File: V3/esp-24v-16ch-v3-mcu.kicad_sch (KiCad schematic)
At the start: 14 parts, among them Q3 UMH3N, SW1 RESET, U3 CH340C, U4 ESP32-WROOM-32UE-N16

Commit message: working on v3
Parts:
- C11: value 10uF/10V/0603 -> 10uF/10V
- C12: value 0,1uF/50V/0805 -> 0,1uF/50V; footprint Tales:C_0805_2012Metric -> Tales:C_0402_1005Metric; Case 0805/2012 -> 0402/1005; LCSC Part # C49678 -> C307331; Mfr Yageo -> Samsung; Mfr PN CC0805KRX7R9BB104 -> CL05B104KB54PNC; Package (none) -> 0402/1005; Technology Ceramic -> Ceramic X7R; Vendor PN C49678 -> C307331
- C13: value 1uF/50V/0603 -> 1uF/25V; footprint Tales:C_0603_1608Metric -> Tales:C_0402_1005Metric; Case 0603/1608 -> 0402/1005; LCSC Part # C15849 -> C52923; Mfr PN CL10A105KB8NNNC -> CL05A105KA5NQNC; Package (none) -> 0402/1005; Vendor PN C15849 -> C52923
- R10, R11, R12: value 10k/62,5mW/0402 -> 10k/62,5mW; LCSC Part # C25744 -> C60490; Mfr Uniroyal -> Yageo; Mfr PN 0402WGF1002TCE -> RC0402FR-0710KL; Package (none) -> 0402/1005; Technology (none) -> 1%; Vendor PN C25744 -> C60490
- R129, R13, R130, R14: value 2k2/62,5mW/0402 -> 2k2/62,5mW
- U4: value ESP32-WROOM-32UE-N16 -> ESP32-WROOM-32UE-N4; LCSC Part # C701346 -> C701344; Mfr PN ESP32-WROOM-32UE-N16 -> ESP32-WROOM-32UE-N4; Vendor PN C701346 -> C701344

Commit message: Final adjustments before production
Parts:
- removed U3: CH340C, Tales:SOIC-16_3.9x9.9mm_P1.27mm, symbol Interface_USB:CH340C
- added U3: CH340C, Package_SO:SOIC-16_3.9x9.9mm_P1.27mm, symbol Tales:CH340C
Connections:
- net +3.3V: now also U3.16 (VCC), U3.4 (V3)
- net GND: now also U3.1 (GND)
- net USB_D+: now also U3.5 (UD+)
- net USB_D-: now also U3.6 (UD-)
- net at Q3.2 (B1), Q3.4 (E2): now also U3.13 (~{DTR})
- net at Q3.1 (E1), Q3.5 (B2): now also U3.14 (~{RTS})
- net at U4.34 (RXD0/IO3): now also U3.2 (TXD)
- net at U4.35 (TXD0/IO1): now also U3.3 (RXD)

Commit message: Added temperature sensor
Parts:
- C12: value 0,1uF/50V -> 100nF/50V
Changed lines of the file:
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@@
 			)
 		)
-		(property "Value" "0,1uF/50V"
+		(property "Value" "100nF/50V"
 			(at 45.72 60.9662 0)
 			(effects

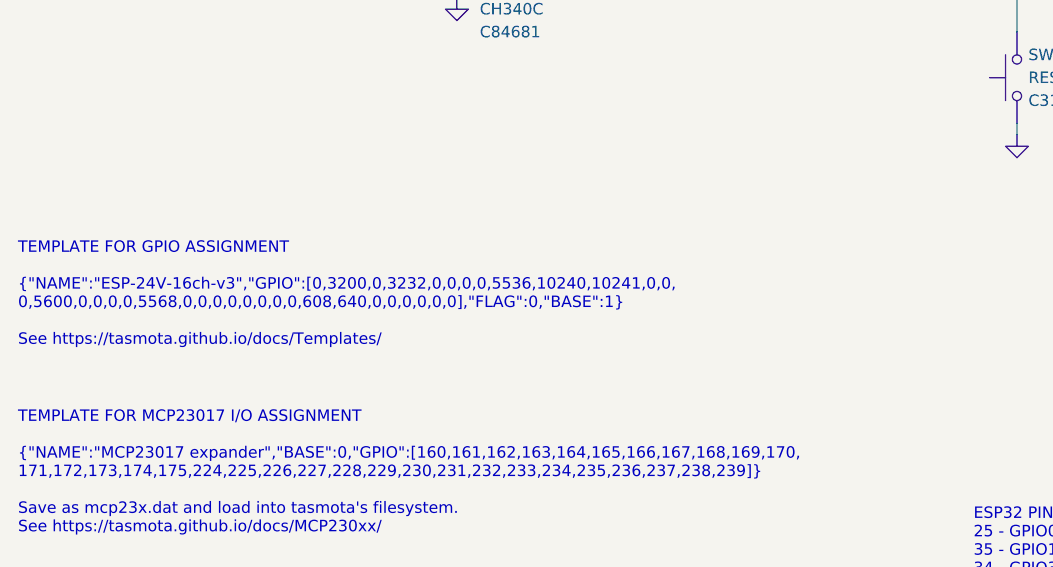
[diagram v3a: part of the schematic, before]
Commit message: Update esp-24v-16ch-v3-mcu.kicad_sch
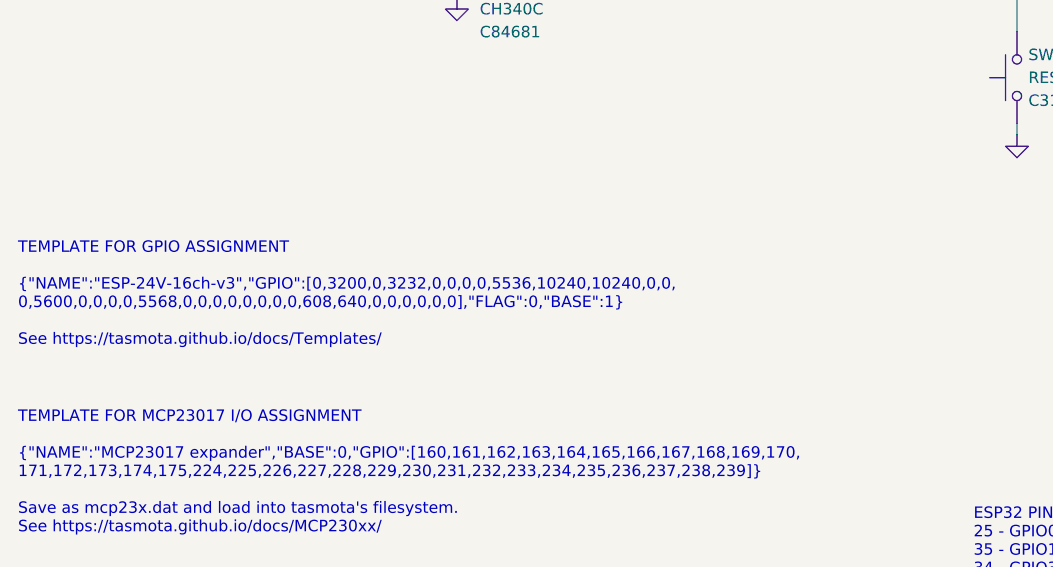
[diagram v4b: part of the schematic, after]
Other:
- note added: "TEMPLATE FOR GPIO ASSIGNMENT {"NAME":"ESP-24V-16ch-v3","GPIO":[0,3200,0,3232,0,0,0,0,5536,10240,10240,0,0, 0,5600,0,0,0,0,5568,0,0,0,0,0,0,0,0,608,640,0,0,0,0,0,0],"FLAG":0,"BASE":1} See https://tasmota.github.io/docs/Templates/"
- note removed: "TEMPLATE FOR GPIO ASSIGNMENT {"NAME":"ESP-24V-16ch-v3","GPIO":[0,3200,0,3232,0,0,0,0,5536,10240,10241,0,0, 0,5600,0,0,0,0,5568,0,0,0,0,0,0,0,0,608,640,0,0,0,0,0,0],"FLAG":0,"BASE":1} See https://tasmota.github.io/docs/Templates/"
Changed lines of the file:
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@@
 		)
 	)
-	(text "TEMPLATE FOR GPIO ASSIGNMENT\n\n{\"NAME\":\"ESP-24V-16ch-v3\",\"GPIO\":[0,3200,0,3232,0,0,0,0,5536,10240,10241,0,0,\n0,5600,0,0,0,0,5568,0,0,0,0,0,0,0,0,608,640,0,0,0,0,0,0],\"FLAG\":0,\"BASE\":1}\n\nSee https://tasmota.github.io/docs/Templates/"
+	(text "TEMPLATE FOR GPIO ASSIGNMENT\n\n{\"NAME\":\"ESP-24V-16ch-v3\",\"GPIO\":[0,3200,0,3232,0,0,0,0,5536,10240,10240,0,0,\n0,5600,0,0,0,0,5568,0,0,0,0,0,0,0,0,608,640,0,0,0,0,0,0],\"FLAG\":0,\"BASE\":1}\n\nSee https://tasmota.github.io/docs/Templates/"
 		(exclude_from_sim no)
 		(at 14.732 141.732 0)

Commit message: Updated footprints
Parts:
- U3: footprint Package_SO:SOIC-16_3.9x9.9mm_P1.27mm -> Tales:SOIC-16_3.9x9.9mm_P1.27mm
- U4: value ESP32-WROOM-32UE-N4 -> ESP32-WROOM-32UE-N16; LCSC Part # C701344 -> C701346; Mfr PN ESP32-WROOM-32UE-N4 -> ESP32-WROOM-32UE-N16; Vendor PN C701344 -> C701346
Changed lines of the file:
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@@
 			)
 		)
-		(property "Footprint" "Package_SO:SOIC-16_3.9x9.9mm_P1.27mm"
+		(property "Footprint" "Tales:SOIC-16_3.9x9.9mm_P1.27mm"
 			(at 44.958 56.134 0)
 			(effects
@@
 			)
 		)
-		(property "Value" "ESP32-WROOM-32UE-N4"
+		(property "Value" "ESP32-WROOM-32UE-N16"
 			(at 182.88 148.59 0)
 			(effects
@@
 			)
 		)
-		(property "LCSC Part #" "C701344"
+		(property "LCSC Part #" "C701346"
 			(at 182.88 151.13 0)
 			(effects
@@
 			)
 		)
-		(property "Mfr PN" "ESP32-WROOM-32UE-N4"
+		(property "Mfr PN" "ESP32-WROOM-32UE-N16"
 			(at 179.07 110.49 0)
 			(effects
@@
 			)
 		)
-		(property "Vendor PN" "C701344"
+		(property "Vendor PN" "C701346 "
 			(at 179.07 110.49 0)
 			(effects

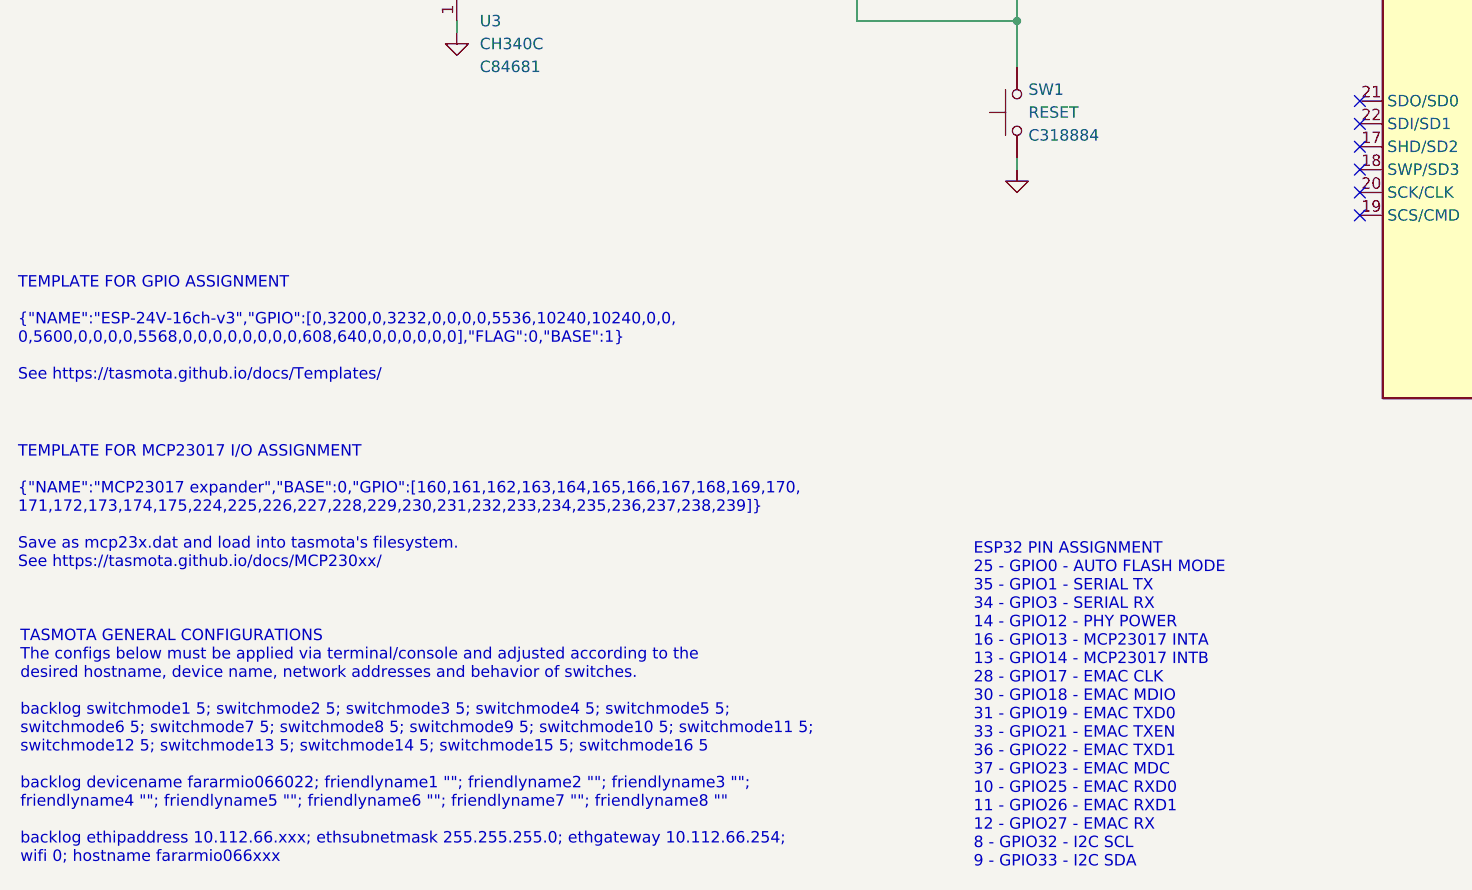
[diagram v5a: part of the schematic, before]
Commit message: Update esp-24v-16ch-v3-mcu.kicad_sch
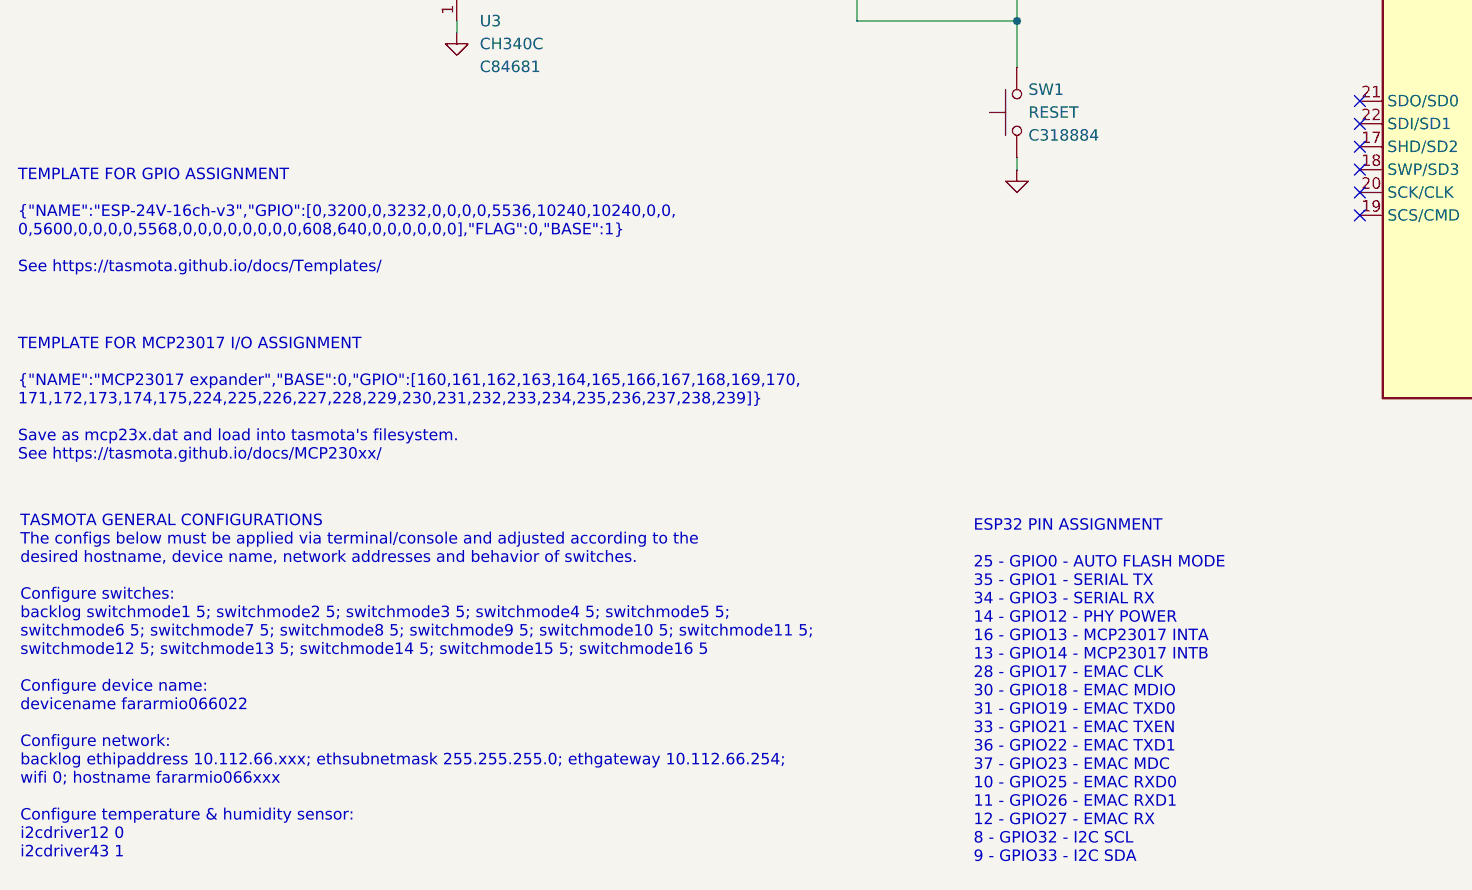
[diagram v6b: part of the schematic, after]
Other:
- note added: "TASMOTA GENERAL CONFIGURATIONS The configs below must be applied via terminal/console and adjusted according to the desired hostname, device name, network addresses and behavior of switches. Configure switches: backlog switchmode1 5; switchmode2 5; switchmode3 5; switchmode4 5; switchmode5 5; switchmode6 5; switchmode7 5; switchmode8 5; switchmode9 5; switchmode10 5; switchmode11 5; switchmode12 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"
- note removed: "TASMOTA GENERAL CONFIGURATIONS The configs below must be applied via terminal/console and adjusted according to the desired hostname, device name, network addresses and behavior of switches. backlog switchmode1 5; switchmode2 5; switchmode3 5; switchmode4 5; switchmode5 5; switchmode6 5; switchmode7 5; switchmode8 5; switchmode9 5; switchmode10 5; switchmode11 5; switchmode12 5; switchmode13 5; s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"
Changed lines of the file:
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@@
 		)
 	)
-	(text "TASMOTA GENERAL CONFIGURATIONS\nThe configs below must be applied via terminal/console and adjusted according to the\ndesired hostname, device name, network addresses and behavior of switches.\n\nbacklog switchmode1 5; switchmode2 5; switchmode3 5; switchmode4 5; switchmode5 5;\nswitchmode6 5; switchmode7 5; switchmode8 5; switchmode9 5; switchmode10 5; switchmode11 5;\nswitchmode12 5; switchmode13 5; switchmode14 5; switchmode15 5; switchmode16 5\n\nbacklog devicename fararmio066022; friendlyname1 \"\"; friendlyname2 \"\"; friendlyname3 \"\";\nfriendlyname4 \"\"; friendlyname5 \"\"; friendlyname6 \"\"; friendlyname7 \"\"; friendlyname8 \"\"\n\nbacklog ethipaddress 10.112.66.xxx; ethsubnetmask 255.255.255.0; ethgateway 10.112.66.254;\nwifi 0; hostname fararmio066xxx"
+	(text "TASMOTA GENERAL CONFIGURATIONS\nThe configs below must be applied via terminal/console and adjusted according to the\ndesired hostname, device name, network addresses and behavior of switches.\n\nConfigure switches:\nbacklog switchmode1 5; switchmode2 5; switchmode3 5; switchmode4 5; switchmode5 5;\nswitchmode6 5; switchmode7 5; switchmode8 5; switchmode9 5; switchmode10 5; switchmode11 5;\nswitchmode12 5; switchmode13 5; switchmode14 5; switchmode15 5; switchmode16 5\n\nConfigure device name:\ndevicename fararmio066022\n\nConfigure network:\nbacklog ethipaddress 10.112.66.xxx; ethsubnetmask 255.255.255.0; ethgateway 10.112.66.254;\nwifi 0; hostname fararmio066xxx\n\nConfigure temperature & humidity sensor:\ni2cdriver12 0\ni2cdriver43 1\n"
 		(exclude_from_sim no)
-		(at 14.986 195.326 0)
+		(at 14.986 194.818 0)
 		(effects
 			(font
@@
 		)
 	)
-	(text "ESP32 PIN ASSIGNMENT\n25 - GPIO0 - AUTO FLASH MODE\n35 - GPIO1 - SERIAL TX\n34 - GPIO3 - SERIAL RX\n14 - GPIO12 - PHY POWER\n16 - GPIO13 - MCP23017 INTA\n13 - GPIO14 - MCP23017 INTB\n28 - GPIO17 - EMAC CLK\n30 - GPIO18 - EMAC MDIO\n31 - GPIO19 - EMAC TXD0\n33 - GPIO21 - EMAC TXEN\n36 - GPIO22 - EMAC TXD1\n37 - GPIO23 - EMAC MDC\n10 - GPIO25 - EMAC RXD0\n11 - GPIO26 - EMAC RXD1\n12 - GPIO27 - EMAC RX\n8 - GPIO32 - I2C SCL\n9 - GPIO33 - I2C SDA"
+	(text "ESP32 PIN ASSIGNMENT\n\n25 - GPIO0 - AUTO FLASH MODE\n35 - GPIO1 - SERIAL TX\n34 - GPIO3 - SERIAL RX\n14 - GPIO12 - PHY POWER\n16 - GPIO13 - MCP23017 INTA\n13 - GPIO14 - MCP23017 INTB\n28 - GPIO17 - EMAC CLK\n30 - GPIO18 - EMAC MDIO\n31 - GPIO19 - EMAC TXD0\n33 - GPIO21 - EMAC TXEN\n36 - GPIO22 - EMAC TXD1\n37 - GPIO23 - EMAC MDC\n10 - GPIO25 - EMAC RXD0\n11 - GPIO26 - EMAC RXD1\n12 - GPIO27 - EMAC RX\n8 - GPIO32 - I2C SCL\n9 - GPIO33 - I2C SDA"
 		(exclude_from_sim no)
-		(at 120.904 195.834 0)
+		(at 120.904 195.326 0)
 		(effects
 			(font
@@
 	(text "TEMPLATE FOR GPIO ASSIGNMENT\n\n{\"NAME\":\"ESP-24V-16ch-v3\",\"GPIO\":[0,3200,0,3232,0,0,0,0,5536,10240,10240,0,0,\n0,5600,0,0,0,0,5568,0,0,0,0,0,0,0,0,608,640,0,0,0,0,0,0],\"FLAG\":0,\"BASE\":1}\n\nSee https://tasmota.github.io/docs/Templates/"
 		(exclude_from_sim no)
-		(at 14.732 141.732 0)
+		(at 14.732 129.794 0)
 		(effects
 			(font
@@
 	(text "TEMPLATE FOR MCP23017 I/O ASSIGNMENT\n\n{\"NAME\":\"MCP23017 expander\",\"BASE\":0,\"GPIO\":[160,161,162,163,164,165,166,167,168,169,170,\n171,172,173,174,175,224,225,226,227,228,229,230,231,232,233,234,235,236,237,238,239]}\n\nSave as mcp23x.dat and load into tasmota's filesystem.\nSee https://tasmota.github.io/docs/MCP230xx/"
 		(exclude_from_sim no)
-		(at 14.732 162.56 0)
+		(at 14.732 150.622 0)
 		(effects
 			(font
